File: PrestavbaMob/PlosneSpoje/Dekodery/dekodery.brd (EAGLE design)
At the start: 100 x 80 mm, 3 parts, among them IC1 ATMEGA48/88/168-AU

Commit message: Prvni verze desky pro dekodery.
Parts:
- added C1, C2, C3, R1, R10, R2, R3, R4, R5, R6, R7, R8, R9: (no value), #PaJa_30:1206
- added CON1: MLW06_90°, #PaJa_konektory:MLW06A
- added D1, D2, D3, D4, D5, D6: LED_SMD_1206, #PaJa_30:P1206
- added K3, K5: (no value), #PaJa_konektory:PSH02-02W
- added K4: (no value), #PaJa_konektory:PSH02-03W
- added Q2: Q_HC-49U_SMD, #PaJa_30:HC-49US
- added T1, T2: BUZ11, ondrap:SOT23
- moved K1 79.4 mm to (41.9, 53.3), turned to 270 degrees
- moved K2 72.7 mm to (17.8, 53.3), turned to 90 degrees
- moved IC1 55.9 mm to (29.2, 41.9)
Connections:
- removed net AGND: IC1.21
- new net N$10: D1.A, IC1.9
- new net N$11: D2.A, IC1.10
- new net N$12: D3.A, IC1.11
- new net N$13: D4.A, IC1.12
- new net N$14: D5.A, IC1.13
- new net N$15: D6.A, IC1.14
- new net N$16: D1.K, R1.1
- new net N$17: D2.K, R2.1
- new net N$18: D3.K, R3.1
- new net N$19: D4.K, R4.1
- new net N$20: D5.K, R5.1
- new net N$21: D6.K, R6.1
- new net N$22: C2.2, IC1.7, Q2.1
- new net N$23: IC1.27, K5.2, R8.1, T2.3
- new net N$24: K4.3, R10.1, R9.2, T1.1, T2.1
- new net N$26: K4.2, R10.2, T2.2
- new net N$27: K4.1, R9.1, T1.2
- new net N$5: IC1.28, K5.1, R7.2, T1.3
- new net N$6: C3.2, IC1.8, Q2.2
- new net N$7: CON1.1, IC1.16
- new net N$8: CON1.3, IC1.17
- new net N$9: CON1.4, IC1.15
- new net RST: CON1.5, IC1.29
- net GND: now also C1.1, C2.1, C3.1, CON1.6, IC1.21, K3.2, R1.2, R2.2, R3.2, R4.2, R5.2, R6.2
- net N$1: now also K2.2; no longer K2.1
- net N$2: now also K2.1; no longer K2.2
- net N$3: now also K1.2; no longer K1.1
- net N$4: now also K1.1; no longer K1.2
- net VCC: now also C1.2, CON1.2, K3.1, R7.1, R8.2
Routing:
- net GND: track 0.00 -> 153.7 mm
- net VCC: track 0.00 -> 117.8 mm, vias 0 -> 2
- net N$5: track 0.00 -> 43.9 mm
- net RST: track 0.00 -> 30.5 mm, vias 0 -> 2
- net N$23: track 0.00 -> 23.1 mm
- net N$24: track 0.00 -> 20.0 mm
- net N$4: track 0.00 -> 19.1 mm
- net N$26: track 0.00 -> 17.6 mm
- net N$6: track 0.00 -> 17.4 mm
- net N$3: track 0.00 -> 17.3 mm
- net N$9: track 0.00 -> 13.9 mm
- net N$1: track 0.00 -> 13.8 mm
- net N$2: track 0.00 -> 11.7 mm
- net N$22: track 0.00 -> 11.6 mm
- net N$8: track 0.00 -> 11.4 mm, vias 0 -> 2
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
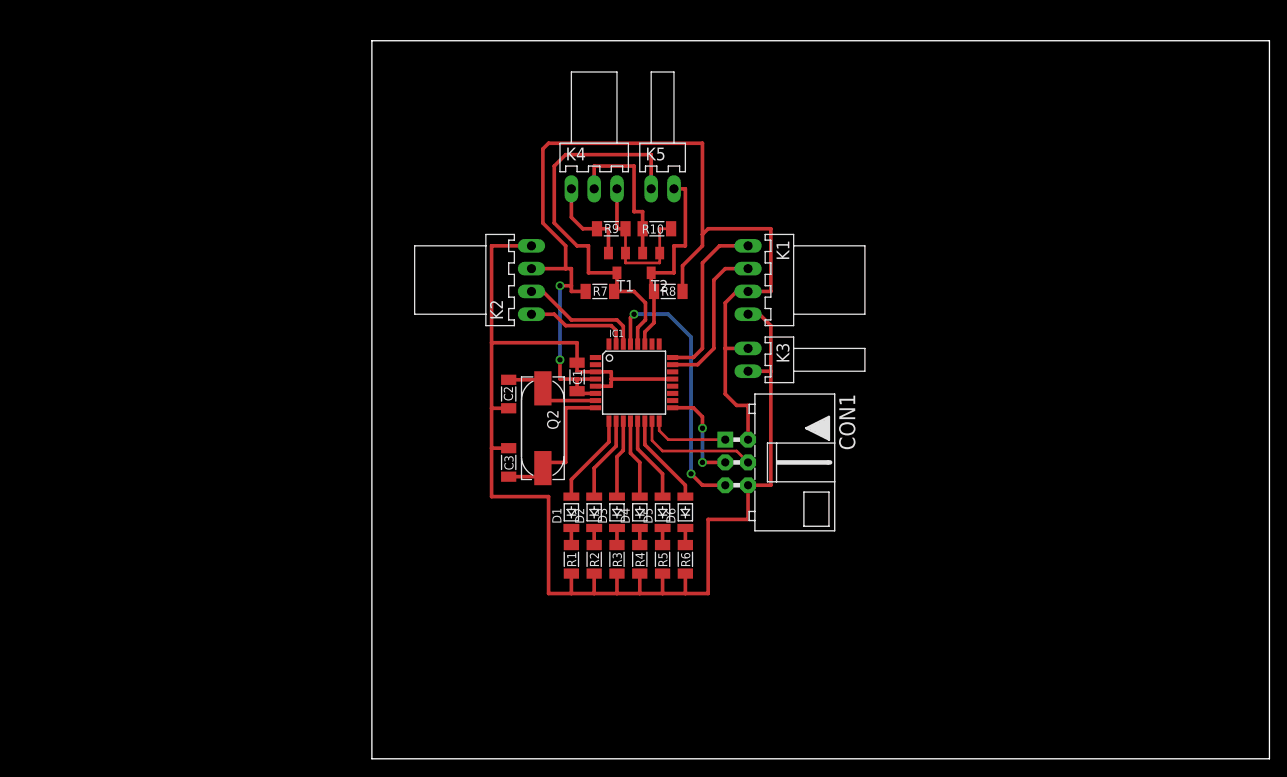
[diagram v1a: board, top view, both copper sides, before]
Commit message: Pridan pull-up rezistor k resetu a zapojeni avcc.
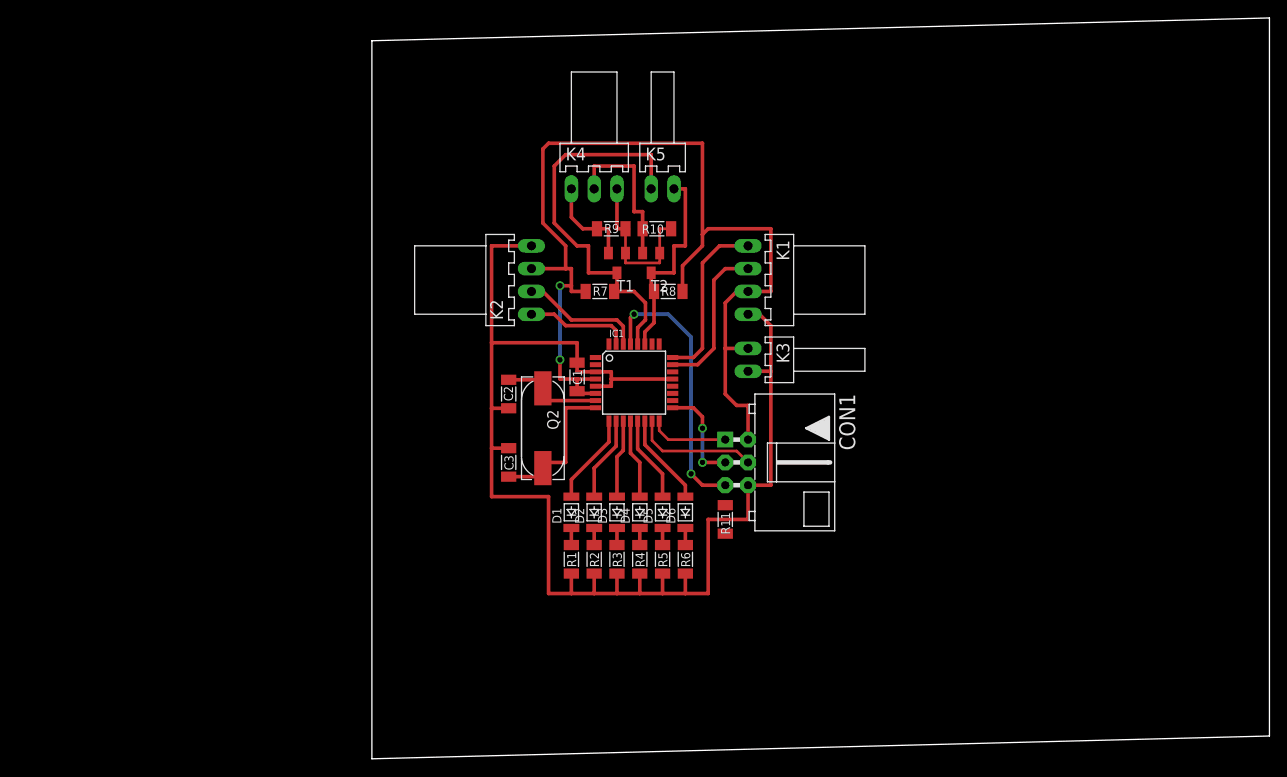
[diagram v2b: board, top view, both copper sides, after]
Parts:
- added R11: 10k, #PaJa_30:1206
- C2: value (none) -> 15pf
- C3: value (none) -> 15p
- R1, R2, R3, R4, R5, R6: value (none) -> 150
- R10, R9: value (none) -> 3.3k
- R7, R8: value (none) -> 4.7k
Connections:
- net RST: now also R11.1
- net VCC: now also IC1.18, R11.2
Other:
- board size 100 x 80 mm -> 100 x 82.5 mm
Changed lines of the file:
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@@
 <board>
 <plain>
-<wire x1="0" y1="0" x2="100" y2="0" width="0" layer="20"/>
-<wire x1="100" y1="0" x2="100" y2="80" width="0" layer="20"/>
-<wire x1="100" y1="80" x2="0" y2="80" width="0" layer="20"/>
+<wire x1="0" y1="0" x2="100" y2="2.54" width="0" layer="20"/>
+<wire x1="100" y1="2.54" x2="100" y2="82.54" width="0" layer="20"/>
+<wire x1="100" y1="82.54" x2="0" y2="80" width="0" layer="20"/>
 <wire x1="0" y1="80" x2="0" y2="0" width="0" layer="20"/>
 </plain>
@@
 <element name="K2" library="#PaJa_konektory" package="PSH02-04W" value="" x="17.78" y="53.34" rot="R90"/>
 <element name="C1" library="#PaJa_30" package="1206" value="" x="22.86" y="42.545" rot="R270"/>
-<element name="C2" library="#PaJa_30" package="1206" value="" x="15.24" y="40.64" rot="R90"/>
-<element name="C3" library="#PaJa_30" package="1206" value="" x="15.24" y="33.02" rot="R270"/>
+<element name="C2" library="#PaJa_30" package="1206" value="15pf" x="15.24" y="40.64" rot="R90"/>
+<element name="C3" library="#PaJa_30" package="1206" value="15p" x="15.24" y="33.02" rot="R270"/>
 <element name="CON1" library="#PaJa_konektory" package="MLW06A" value="MLW06_90°" x="40.64" y="33.02" rot="R270"/>
 <element name="D1" library="#PaJa_30" package="P1206" value="LED_SMD_1206" x="22.225" y="27.305" rot="R270"/>
@@
 <element name="D5" library="#PaJa_30" package="P1206" value="LED_SMD_1206" x="32.385" y="27.305" rot="R270"/>
 <element name="D6" library="#PaJa_30" package="P1206" value="LED_SMD_1206" x="34.925" y="27.305" rot="R270"/>
-<element name="R1" library="#PaJa_30" package="1206" value="" x="22.225" y="22.225" rot="R270"/>
-<element name="R2" library="#PaJa_30" package="1206" value="" x="24.765" y="22.225" rot="R270"/>
-<element name="R3" library="#PaJa_30" package="1206" value="" x="27.305" y="22.225" rot="R270"/>
-<element name="R4" library="#PaJa_30" package="1206" value="" x="29.845" y="22.225" rot="R270"/>
-<element name="R5" library="#PaJa_30" package="1206" value="" x="32.385" y="22.225" rot="R270"/>
-<element name="R6" library="#PaJa_30" package="1206" value="" x="34.925" y="22.225" rot="R270"/>
+<element name="R1" library="#PaJa_30" package="1206" value="150" x="22.225" y="22.225" rot="R270"/>
+<element name="R2" library="#PaJa_30" package="1206" value="150" x="24.765" y="22.225" rot="R270"/>
+<element name="R3" library="#PaJa_30" package="1206" value="150" x="27.305" y="22.225" rot="R270"/>
+<element name="R4" library="#PaJa_30" package="1206" value="150" x="29.845" y="22.225" rot="R270"/>
+<element name="R5" library="#PaJa_30" package="1206" value="150" x="32.385" y="22.225" rot="R270"/>
+<element name="R6" library="#PaJa_30" package="1206" value="150" x="34.925" y="22.225" rot="R270"/>
 <element name="K3" library="#PaJa_konektory" package="PSH02-02W" value="" x="41.91" y="44.45" rot="R270"/>
 <element name="Q2" library="#PaJa_30" package="HC-49US" value="Q_HC-49U_SMD" x="19.05" y="36.83" rot="R270"/>
@@
 <element name="T2" library="ondrap" package="SOT23" value="BUZ11" x="31.115" y="55.245" rot="R180"/>
 <element name="K4" library="#PaJa_konektory" package="PSH02-03W" value="" x="24.765" y="63.5"/>
-<element name="R7" library="#PaJa_30" package="1206" value="" x="25.4" y="52.07"/>
-<element name="R8" library="#PaJa_30" package="1206" value="" x="33.02" y="52.07"/>
-<element name="R9" library="#PaJa_30" package="1206" value="" x="26.67" y="59.055"/>
-<element name="R10" library="#PaJa_30" package="1206" value="" x="31.75" y="59.055" rot="R180"/>
+<element name="R7" library="#PaJa_30" package="1206" value="4.7k" x="25.4" y="52.07"/>
+<element name="R8" library="#PaJa_30" package="1206" value="4.7k" x="33.02" y="52.07"/>
+<element name="R9" library="#PaJa_30" package="1206" value="3.3k" x="26.67" y="59.055"/>
+<element name="R10" library="#PaJa_30" package="1206" value="3.3k" x="31.75" y="59.055" rot="R180"/>
 <element name="K5" library="#PaJa_konektory" package="PSH02-02W" value="" x="32.385" y="63.5"/>
+<element name="R11" library="#PaJa_30" package="1206" value="10k" x="39.37" y="26.67" rot="R270"/>
 </elements>
 <signals>
@@
 <wire x1="19.05" y1="59.69" x2="21.59" y2="57.15" width="0.4064" layer="1"/>
 <wire x1="21.59" y1="57.15" x2="21.59" y2="54.61" width="0.4064" layer="1"/>
+<contactref element="R11" pad="2"/>
+<contactref element="IC1" pad="18"/>
+<wire x1="39.37" y1="40.64" x2="33.5026" y2="39.91" width="0" layer="19" extent="1-1"/>
+<wire x1="39.37" y1="25.0825" x2="41.91" y2="35.56" width="0" layer="19" extent="1-1"/>
 </signal>
 <signal name="N$3">
@@
 <wire x1="35.56" y1="31.75" x2="36.83" y2="30.48" width="0.4064" layer="1"/>
 <wire x1="36.83" y1="30.48" x2="39.37" y2="30.48" width="0.4064" layer="1"/>
+<contactref element="R11" pad="1"/>
+<wire x1="39.37" y1="28.2575" x2="36.83" y2="30.48" width="0" layer="19" extent="1-1"/>
 </signal>
 <signal name="N$10">
@@
 <wire x1="29.61" y1="46.2026" x2="29.61" y2="48.025" width="0.4064" layer="1"/>
 <wire x1="31.115" y1="63.5" x2="31.115" y2="67.31" width="0.4064" layer="1"/>
-<wire x1="20.32" y1="67.31" x2="21.59" y2="67.31" width="0" layer="19" extent="1-16"/>
 <wire x1="21.59" y1="67.31" x2="31.115" y2="67.31" width="0.4064" layer="1"/>
 <wire x1="24.13" y1="57.15" x2="24.13" y2="54.145" width="0.4064" layer="1"/>

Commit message: Upravena deska pro dekodery. Rozpracovano zapojeni soucastek a jejich propojeni na desce.
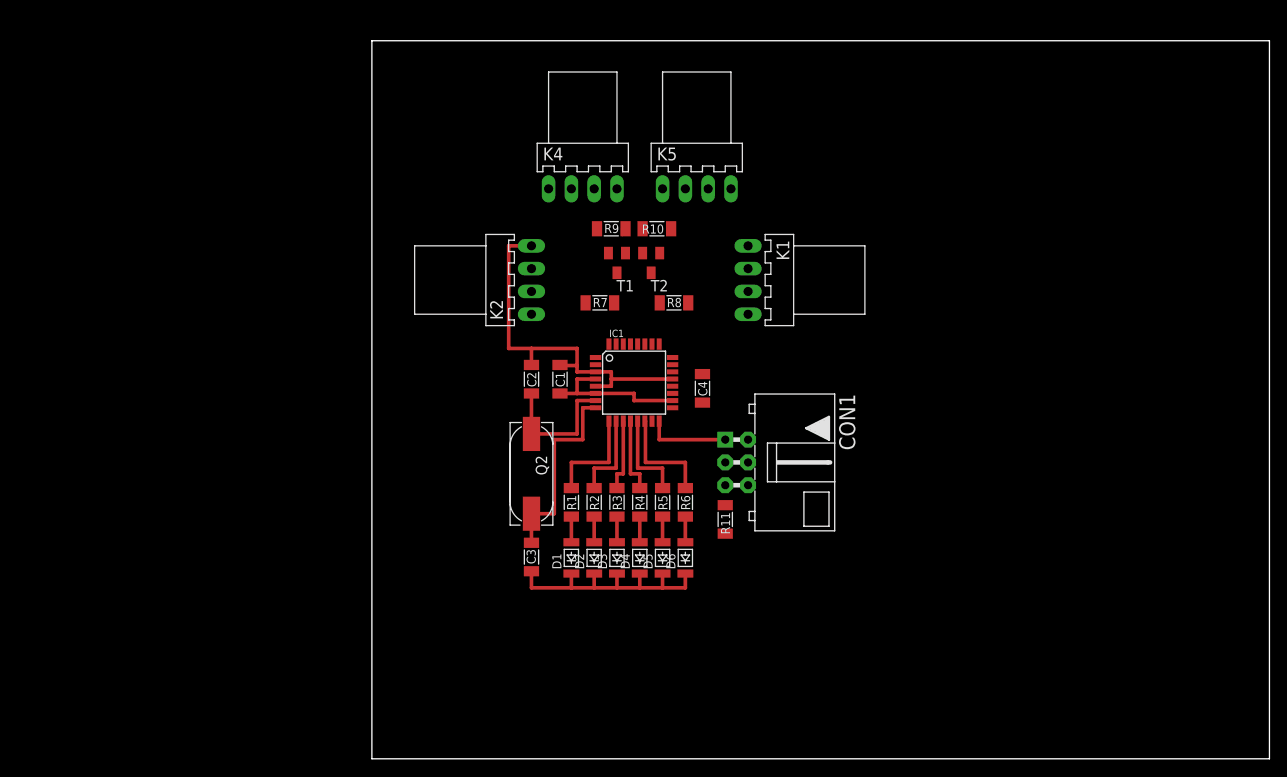
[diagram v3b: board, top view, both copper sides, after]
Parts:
- removed K3: (no value), #PaJa_konektory:PSH02-02W
- added C4: (no value), #PaJa_30:1206
- K4: device #PaJa_konektory:PSH02-03W -> #PaJa_konektory:PSH02-04W
- K5: device #PaJa_konektory:PSH02-02W -> #PaJa_konektory:PSH02-04W
- moved C3 10.8 mm to (17.8, 22.5), turned to 90 degrees
- moved R1 6.35 mm to (22.2, 28.6)
- moved R2 6.35 mm to (24.8, 28.6)
- moved R3 6.35 mm to (27.3, 28.6)
- moved R4 6.35 mm to (29.8, 28.6)
- moved R5 6.35 mm to (32.4, 28.6)
- moved R6 6.35 mm to (34.9, 28.6)
- moved Q2 5.24 mm to (17.8, 31.8)
- moved D1 5.08 mm to (22.2, 22.2)
- moved D2 5.08 mm to (24.8, 22.2)
- moved D3 5.08 mm to (27.3, 22.2)
- moved D4 5.08 mm to (29.8, 22.2)
- moved D5 5.08 mm to (32.4, 22.2)
- moved D6 5.08 mm to (34.9, 22.2)
- moved K5 3.81 mm to (36.2, 63.5)
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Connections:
- net GND: now also C4.1, D1.K, D2.K, D3.K, D4.K, D5.K, D6.K, K4.4, K5.4; no longer K3.2, R1.2, R2.2, R3.2, R4.2, R5.2, R6.2
- net N$10: now also R1.1; no longer D1.A
- net N$11: now also R2.1; no longer D2.A
- net N$12: now also R3.1; no longer D3.A
- net N$13: now also R4.1; no longer D4.A
- net N$14: now also R5.1; no longer D5.A
- net N$15: now also R6.1; no longer D6.A
- net N$16: now also D1.A, R1.2; no longer D1.K, R1.1
- net N$17: now also D6.A, R6.2; no longer D2.K, R2.1
- net N$18: now also D5.A, R5.2; no longer D3.K, R3.1
- net N$19: now also D4.A, R4.2; no longer D4.K, R4.1
- net N$20: now also D3.A, R3.2; no longer D5.K, R5.1
- net N$21: now also D2.A, R2.2; no longer D6.K, R6.1
- net VCC: now also C4.2, K5.3; no longer K3.1
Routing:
- net VCC: track 117.8 -> 17.0 mm, vias 2 -> 0
- net GND: track 153.7 -> 70.5 mm
- net N$5: track 43.9 -> 0.00 mm
- net RST: track 30.5 -> 0.00 mm, vias 2 -> 0
- net N$23: track 23.1 -> 0.00 mm
- net N$4: track 19.1 -> 0.00 mm
- net N$24: track 20.0 -> 1.27 mm
- net N$26: track 17.6 -> 0.00 mm
- net N$3: track 17.3 -> 0.00 mm
- net N$9: track 13.9 -> 0.00 mm
- net N$1: track 13.8 -> 0.00 mm
- net N$2: track 11.7 -> 0.00 mm
- net N$8: track 11.4 -> 0.00 mm, vias 2 -> 0
- net N$27: track 10.5 -> 0.00 mm
- net N$6: track 17.4 -> 22.2 mm
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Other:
- board size 100 x 82.5 mm -> 100 x 80 mm

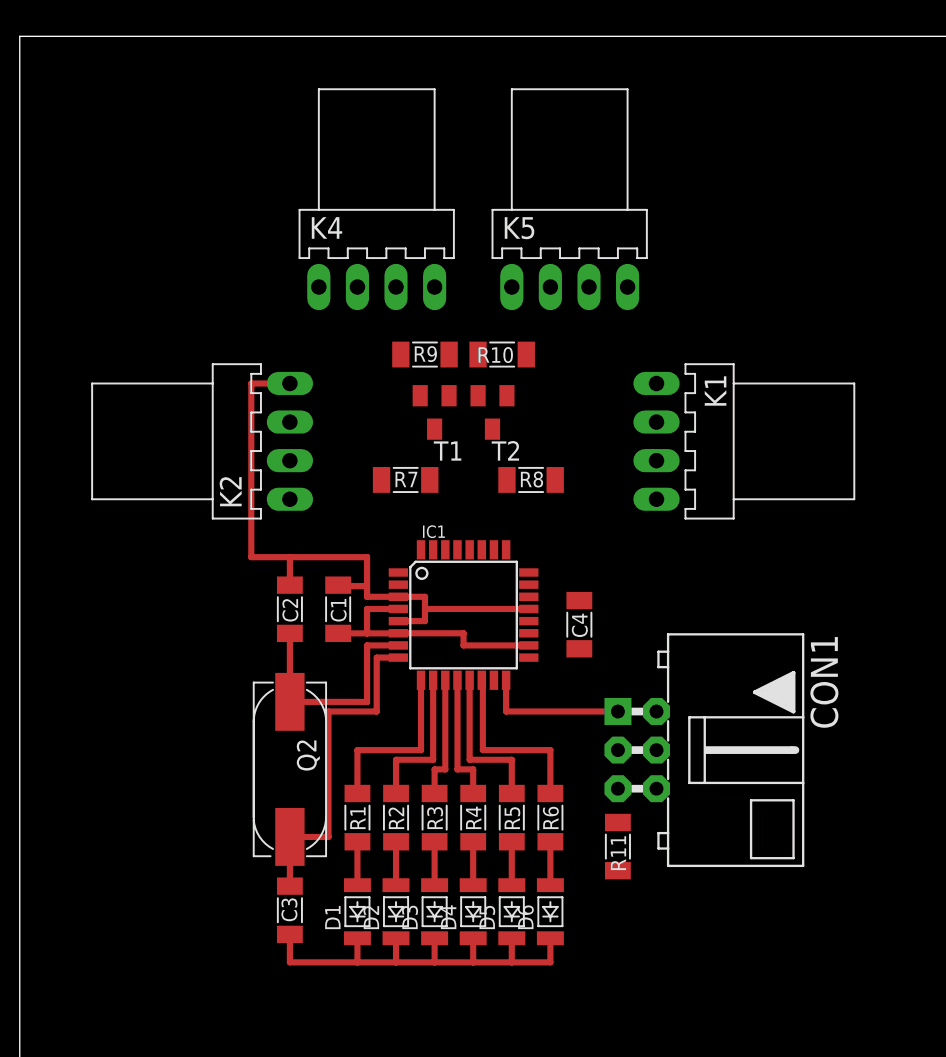
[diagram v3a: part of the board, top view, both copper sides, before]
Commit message: Druha verze navrhu desky s propojenim vsech soucastek.
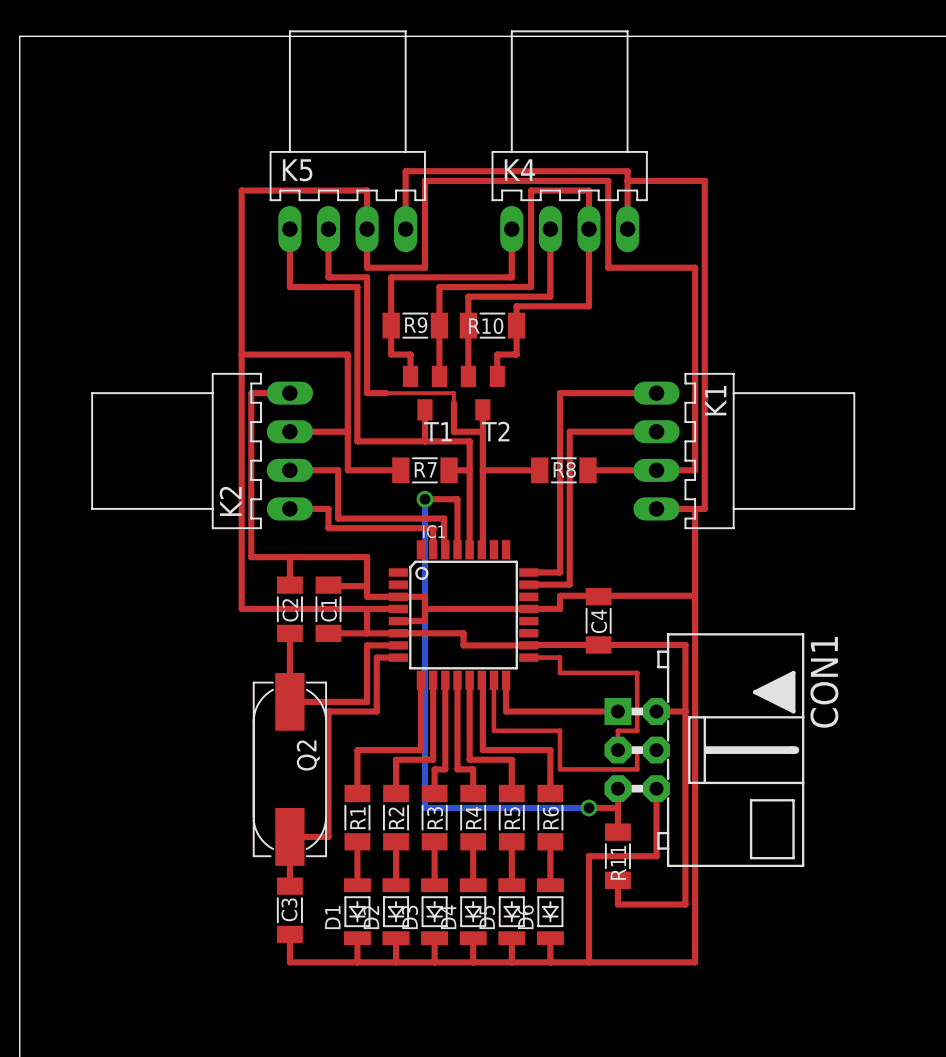
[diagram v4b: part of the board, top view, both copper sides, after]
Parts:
- moved K5 15.1 mm to (21.6, 67.3)
- moved K4 13.3 mm to (36.2, 67.3)
- moved R8 2.25 mm to (35.8, 51.4)
- moved R10 2.01 mm to (31.1, 61.0)
- moved R9 2.01 mm to (26.0, 61.0)
- moved R7 1.42 mm to (26.7, 51.4)
- moved T1 1.42 mm to (26.7, 56.5)
- moved T2 1.42 mm to (30.5, 56.5)
- moved C4 1.30 mm to (38.1, 41.5)
- moved K1 0.64 mm to (41.9, 52.7)
- moved K2 0.64 mm to (17.8, 52.7)
- moved R11 0.64 mm to (39.4, 26.0)
- moved C1 0.63 mm to (20.3, 42.3)
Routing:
- net VCC: track 17.0 -> 177.5 mm
- net GND: track 70.5 -> 189.7 mm
- net RST: track 0.00 -> 41.3 mm, vias 0 -> 2
- net N$24: track 1.27 -> 41.9 mm
- net N$23: track 0.00 -> 36.5 mm
- net N$5: track 0.00 -> 36.4 mm
- net N$4: track 0.00 -> 20.2 mm
- net N$27: track 0.00 -> 19.2 mm
- net N$3: track 0.00 -> 18.5 mm
- net N$9: track 0.00 -> 17.8 mm
- net N$1: track 0.00 -> 15.5 mm
- net N$26: track 0.00 -> 15.1 mm
- net N$8: track 0.00 -> 14.5 mm
- net N$2: track 0.00 -> 12.2 mm
